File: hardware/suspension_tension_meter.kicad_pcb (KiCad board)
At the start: 2 copper layers, 63 parts, among them J1 Conn_01x04, J2 Conn_01x06, J3 Conn_01x04, J4 Conn_01x04, SW1 Tactswitch, U1 STM32L4P5RET6, U2 LM2596S-ADJ, U3 LM1117-5.0, U4 LM1117-3.3, U5 NAU7802SGI, U6 ATA6561, U7 NAU7802SGI, Y1 16MHz

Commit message: Arrange footprints
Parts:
- removed JP1: Terminator, Connector_PinHeader_2.54mm:PinHeader_1x02_P2.54mm_Vertical
- added C30: 1μF, Capacitor_SMD:C_0603_1608Metric, F.Cu at (171.3, 126.4)
- added J5: Terminator, Connector_PinHeader_2.54mm:PinHeader_1x02_P2.54mm_Vertical_SMD_Pin1Left, F.Cu at (127.4, 97.0)
- added R15: 51Ω, Resistor_SMD:R_0603_1608Metric, F.Cu at (175.2, 121.8)
- added REF**: MountingHole_4mm_Pad_Via, MountingHole:MountingHole_4mm_Pad_Via, F.Cu at (112.0, 84.0)
- added REF**: MountingHole_4mm_Pad_Via, MountingHole:MountingHole_4mm_Pad_Via, F.Cu at (186.0, 126.0)
- added REF**: MountingHole_4mm_Pad_Via, MountingHole:MountingHole_4mm_Pad_Via, F.Cu at (186.0, 84.0)
- added REF**: MountingHole_4mm_Pad_Via, MountingHole:MountingHole_4mm_Pad_Via, F.Cu at (112.0, 126.0)
- C1, C2: value 22pF -> 100nF
- C10: value 220μF -> 10nF; footprint Capacitor_SMD:CP_Elec_10x10 -> Capacitor_SMD:C_0603_1608Metric
- C11: value 100nF -> 10μF; footprint Capacitor_SMD:C_0603_1608Metric -> Capacitor_SMD:C_Elec_4x5.4
- C19: value 10μF -> 100nF; footprint Capacitor_SMD:CP_Elec_5x5.4 -> Capacitor_SMD:C_0603_1608Metric
- C20: value 100nF -> 10μF
- C24: value 470pF -> 100nF
- C26: value 100nF -> 470pF
- C29: value 1μF -> 100nF
- C7, C8: value 100nF -> 22pF
- C9: value 680μF -> 4.7μF; footprint Capacitor_SMD:CP_Elec_10x10 -> Capacitor_SMD:C_Elec_4x5.4
- D1: value 1N5822 -> SK32SMA; footprint Diode_THT:D_DO-201AD_P15.24mm_Horizontal -> Diode_SMD:D_SMA
- F1: footprint Fuse:Fuse_0603_1608Metric -> Fuse:Fuse_1210_3225Metric
- FB1, FB2: value 60R@100MHz -> 50mΩ@100MHz; footprint Inductor_SMD:L_0603_1608Metric -> Inductor_SMD:L_1206_3216Metric
- J1: footprint Connector_PinHeader_1.00mm:PinHeader_1x04_P1.00mm_Vertical_SMD_Pin1Left -> Connector_Wire:SolderWire-0.25sqmm_1x04_P4.2mm_D0.65mm_OD1.7mm_Relief
- J2: footprint Connector_PinHeader_1.00mm:PinHeader_1x06_P1.00mm_Vertical_SMD_Pin1Left -> Connector_PinHeader_2.54mm:PinHeader_1x06_P2.54mm_Vertical_SMD_Pin1Left
- J3, J4: footprint Connector_PinHeader_1.00mm:PinHeader_1x04_P1.00mm_Vertical_SMD_Pin1Left -> Connector_JST:JST_EH_S5B-EH_1x05_P2.50mm_Horizontal
- L1: value 33μH -> 2.2μH; footprint Inductor_SMD:L_0805_2012Metric -> Inductor_SMD:L_Bourns-SRN4018
- R1: value 100kΩ -> 330Ω
- R10, R9: value 51Ω -> 10kΩ
- R12: value 10kΩ -> 51Ω
- R3: value 330Ω -> 100kΩ
- R4: value 4.7kΩ -> 10kΩ
- R5: value 1kΩ -> 33kΩ
- R6: value 120Ω -> 4.7kΩ
- R7: value 10kΩ -> 120Ω
- SW1: footprint Button_Switch_SMD:SW_Push_1P1T_NO_6x6mm_H9.5mm -> Button_Switch_SMD:SW_SPST_PTS645
- U2: value LM2596S-ADJ -> AOZ1280CI; footprint Package_TO_SOT_SMD:TO-263-5_TabPin3 -> Package_TO_SOT_SMD:SOT-23-6
- U3, U4: footprint Package_TO_SOT_SMD:SOT-223 -> Package_TO_SOT_SMD:SOT-223-3_TabPin2
- U5: value NAU7802SGI -> ATA6561-GAQW-N; footprint Package_SO:SOIC-16_3.9x9.9mm_P1.27mm -> Package_SO:SOIC-8_3.9x4.9mm_P1.27mm
- U6: value ATA6561 -> NAU7802SGI; footprint Package_SO:SOIC-8_3.9x4.9mm_P1.27mm -> Package_SO:SOIC-16_3.9x9.9mm_P1.27mm
- moved J4 81.5 mm to (184.8, 100.0), turned to -90 degrees
- moved U4 75.4 mm to (176.2, 87.7)
- moved R13 71.6 mm to (121.3, 117.5), turned to 180 degrees
- moved C23 69.4 mm to (122.0, 123.8), turned to -90 degrees
- moved R12 68.4 mm to (121.3, 115.5), turned to 180 degrees
- moved C18 65.7 mm to (132.5, 116.0), turned to -90 degrees
- moved R10 65.0 mm to (132.5, 123.3), turned to 90 degrees
- moved C28 63.0 mm to (125.0, 112.9)
- moved C14 62.6 mm to (170.3, 86.0), turned to -90 degrees
- moved C25 59.3 mm to (122.0, 120.3), turned to -90 degrees
- moved C13 58.5 mm to (170.3, 89.8), turned to 90 degrees
- moved R8 57.6 mm to (132.5, 119.5), turned to -90 degrees
- moved J2 57.2 mm to (170.3, 107.7), turned to -90 degrees
- moved SW1 56.1 mm to (172.0, 98.6)
- moved C20 55.8 mm to (149.5, 124.9)
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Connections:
- C1 pad 1: Net-(C1-Pad1) -> +3.3V
- C10 pad 2: GND -> Net-(C10-Pad2)
- C11 pad 1: Net-(C10-Pad1) -> /Power Supply/6.42V
- C12 pad 1: +5V -> /Power Supply/6.42V
- C14 pad 1: +3.3V -> +5V
- C15 pad 1: Net-(C15-Pad1) -> +3.3V
- C17 pad 1: +3.3V -> Net-(C17-Pad1)
- C2 pad 1: Net-(C2-Pad1) -> +3.3V
- C22 pad 1: Net-(C22-Pad1) -> +3.3V
- C24 pad 2: Net-(C24-Pad2) -> GND
- C26 pad 1: /A1+ -> Net-(C26-Pad1)
- C26 pad 2: /A1- -> Net-(C26-Pad2)
- C27 pad 1: /A2+ -> /A1+
- C27 pad 2: /A2- -> /A1-
- C29 pad 1: +3.3V -> /A2+
- C29 pad 2: GND -> /A2-
- C3 pad 1: /NRST -> +3.3V
- C6 pad 1: +3.3V -> /NRST
- C7 pad 1: +3.3V -> Net-(C7-Pad1)
- C8 pad 1: +3.3V -> Net-(C8-Pad1)
- D1 pad 1: Net-(D1-Pad1) -> Net-(C10-Pad2)
- FB1 pad 1: +5V -> +3.3V
- FB2 pad 1: +3.3V -> +5V
- FB2 pad 2: Net-(C15-Pad1) -> Net-(C17-Pad1)
- J2 pad 6: unconnected-(J2-Pad6) -> /SWO
- L1 pad 1: Net-(D1-Pad1) -> Net-(C10-Pad2)
- L1 pad 2: Net-(C10-Pad1) -> /Power Supply/6.42V
- R1 pad 1: GND -> /NRST
- R10 pad 1: Net-(R10-Pad1) -> +3.3V
- R10 pad 2: /A1- -> /SCLK1
- R11 pad 2: /SDIO2 -> /SCLK2
- R12 pad 1: +3.3V -> Net-(R12-Pad1)
- R12 pad 2: /SCLK2 -> /A1+
- R13 pad 2: /A2+ -> /A1-
- R14 pad 2: /A2- -> /A2+
- R3 pad 1: /NRST -> GND
- R4 pad 1: Net-(C10-Pad1) -> Net-(C9-Pad1)
- R5 pad 1: Net-(R4-Pad2) -> /Power Supply/6.42V
- R5 pad 2: GND -> /Power Supply/FB
- R6 pad 1: Net-(JP1-Pad2) -> /Power Supply/FB
- R6 pad 2: /CAN- -> GND
- R7 pad 1: +3.3V -> Net-(J5-Pad2)
- R7 pad 2: /SDIO1 -> /CAN-
- R8 pad 2: /SCLK1 -> /SDIO1
- R9 pad 1: Net-(R9-Pad1) -> +3.3V
- R9 pad 2: /A1+ -> /SDIO2
- SW1 pad 2: Net-(R3-Pad2) -> Net-(R1-Pad2)
- U1 pad 5: Net-(C1-Pad1) -> Net-(C7-Pad1)
- U1 pad 55: unconnected-(U1-Pad55) -> /SWO
- U1 pad 6: Net-(C2-Pad1) -> Net-(C8-Pad1)
- U1 pad 60: Net-(R1-Pad2) -> Net-(R3-Pad2)
- U2 pad 1: Net-(C9-Pad1) -> Net-(C10-Pad1)
- U2 pad 2: Net-(D1-Pad1) -> GND
- U2 pad 3: GND -> /Power Supply/FB
- U2 pad 5: GND -> Net-(C9-Pad1)
- U3 pad 3: Net-(C10-Pad1) -> /Power Supply/6.42V
- U5 pad 1: +3.3V -> /CAN_TX
- U5 pad 2: Net-(R9-Pad1) -> GND
- U5 pad 3: Net-(R10-Pad1) -> Net-(C17-Pad1)
- U5 pad 4: Net-(C24-Pad1) -> /CAN_RX
- U5 pad 5: Net-(C24-Pad2) -> Net-(C16-Pad1)
- U5 pad 6: Net-(C22-Pad1) -> /CAN-
- U5 pad 7: GND -> /CAN+
- U6 pad 1: /CAN_TX -> +3.3V
- U6 pad 2: GND -> Net-(R12-Pad1)
- U6 pad 3: Net-(C16-Pad1) -> Net-(R13-Pad1)
- U6 pad 4: /CAN_RX -> Net-(C25-Pad1)
- U6 pad 5: Net-(C15-Pad1) -> Net-(C25-Pad2)
- U6 pad 6: /CAN- -> Net-(C23-Pad1)
- U6 pad 7: /CAN+ -> GND
- U7 pad 2: Net-(R13-Pad1) -> Net-(R14-Pad1)
- U7 pad 3: Net-(R14-Pad1) -> Net-(R15-Pad1)
- U7 pad 4: Net-(C25-Pad1) -> Net-(C26-Pad1)
- U7 pad 5: Net-(C25-Pad2) -> Net-(C26-Pad2)
- U7 pad 6: Net-(C23-Pad1) -> Net-(C24-Pad1)
- Y1 pad 1: Net-(C2-Pad1) -> Net-(C8-Pad1)
- Y1 pad 3: Net-(C1-Pad1) -> Net-(C7-Pad1)
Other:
- board outline added: 86 x 54 mm
- board text added: "LEFT"
- board text added: "RIGHT"
- board text added: "Rev: ${REVISION}"
- board text added: "Suspension Tension Meter"
- board text added: "‹Per aspera ad astra›"

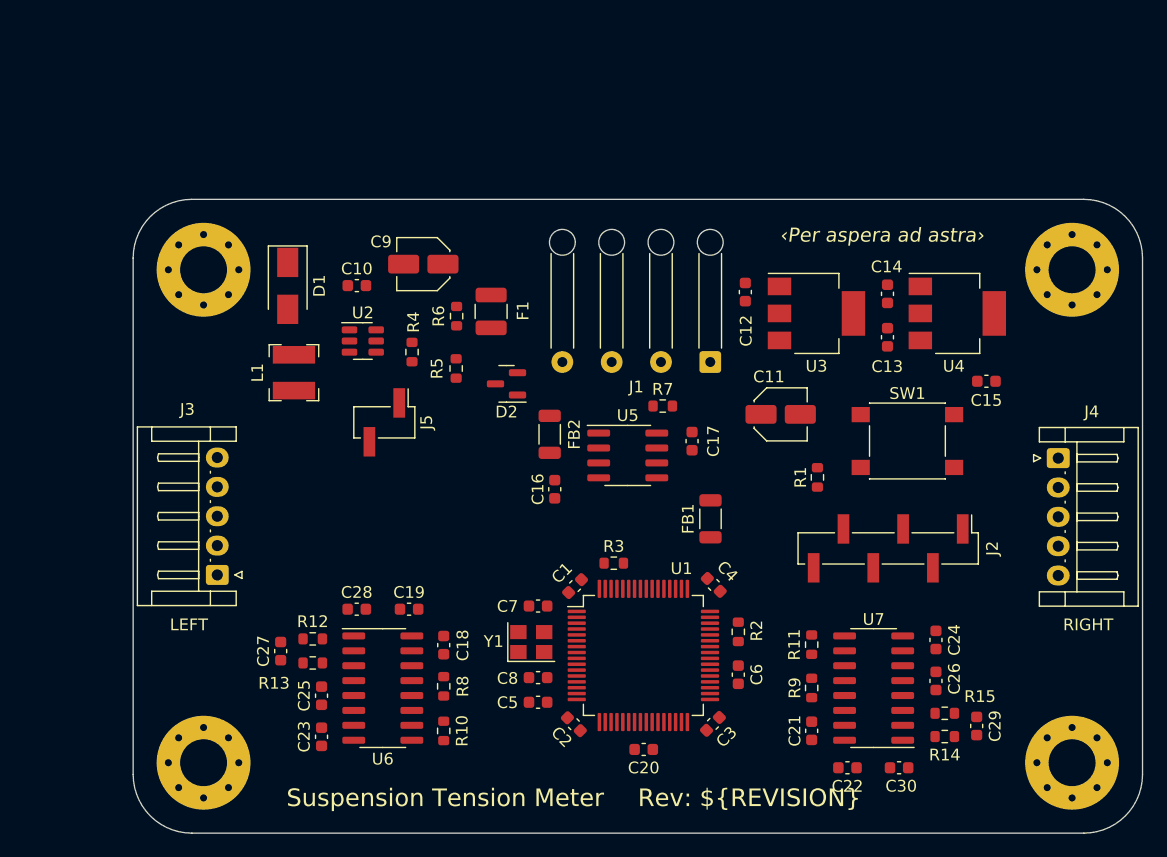
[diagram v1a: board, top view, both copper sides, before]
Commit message: Make the PCB more compact
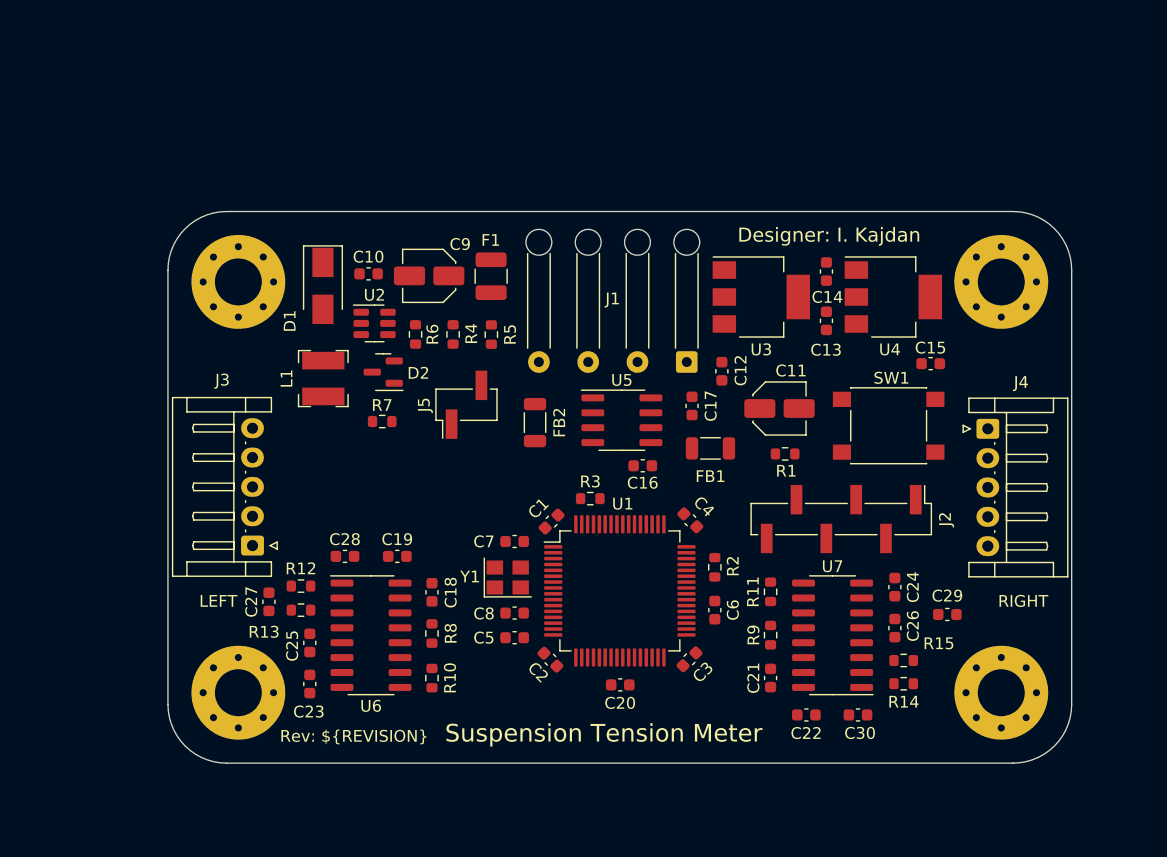
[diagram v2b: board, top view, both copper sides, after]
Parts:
- moved REF** 41.4 mm to (180.0, 85.0)
- moved REF** 36.5 mm to (180.0, 120.0)
- moved R7 23.9 mm to (127.2, 96.9), turned to 180 degrees
- moved D2 10.5 mm to (127.3, 92.7)
- moved C29 9.82 mm to (175.4, 113.4), turned to 180 degrees
- moved C16 7.76 mm to (149.4, 100.7), turned to 180 degrees
- moved J5 7.16 mm to (134.4, 95.5), turned to 90 degrees
- moved C12 7.04 mm to (156.2, 92.7), turned to -90 degrees
- moved REF** 6.66 mm to (115.0, 120.0)
- moved J4 6.50 mm to (178.8, 97.5)
- moved FB1 6.00 mm to (155.2, 99.2), turned to 180 degrees
- moved C1 5.85 mm to (141.7, 105.5)
- moved C2 5.85 mm to (141.6, 117.2)
- moved C20 5.85 mm to (147.5, 119.4)
- moved C3 5.85 mm to (153.4, 117.2)
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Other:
- board size 86 x 54 mm -> 77 x 47 mm
- board text added: "Designer: I. Kajdan"
- board text removed: "‹Per aspera ad astra›"

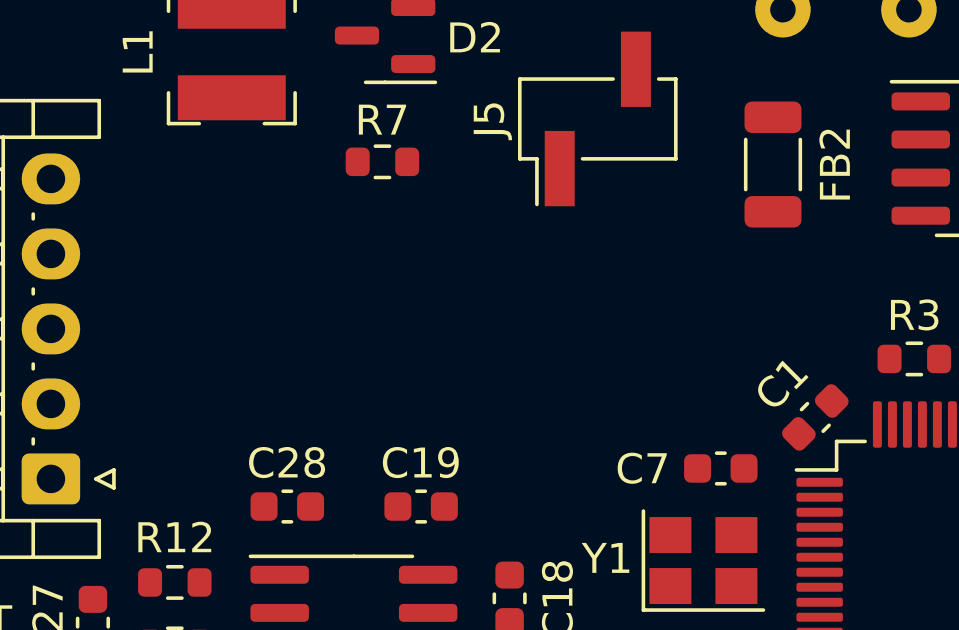
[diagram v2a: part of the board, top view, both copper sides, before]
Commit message: Apply PUTM branding
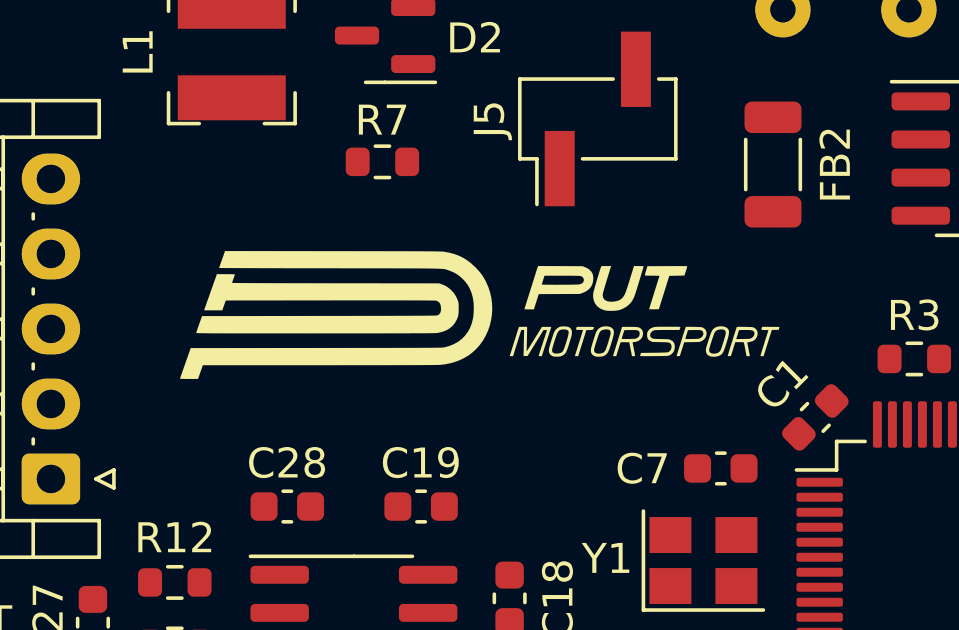
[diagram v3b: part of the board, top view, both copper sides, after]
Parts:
- added G***: LOGO, Local_Library:putm_text_20mm, F.Cu at (130.5, 102.0)

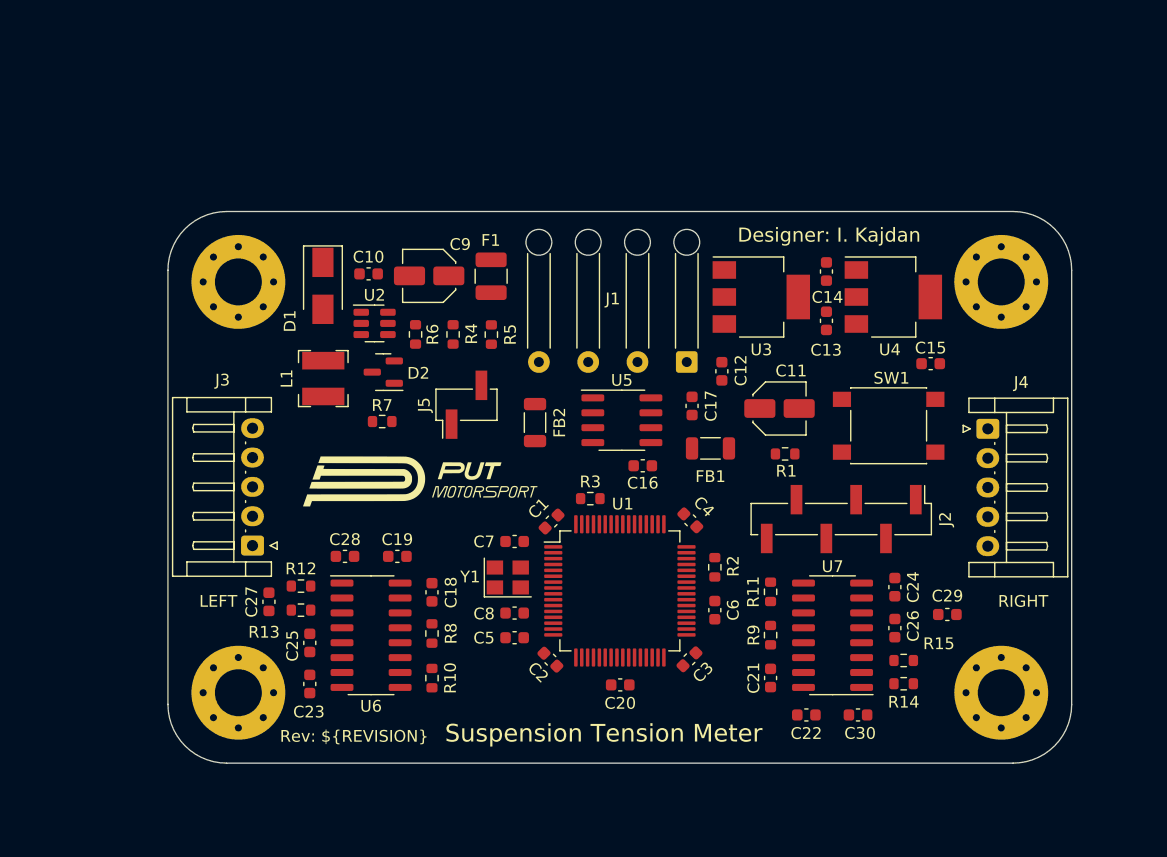
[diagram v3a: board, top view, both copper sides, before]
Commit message: Miscellaneous changes
- Use THT connectors
- Adjust ADC circuit according to the datasheet
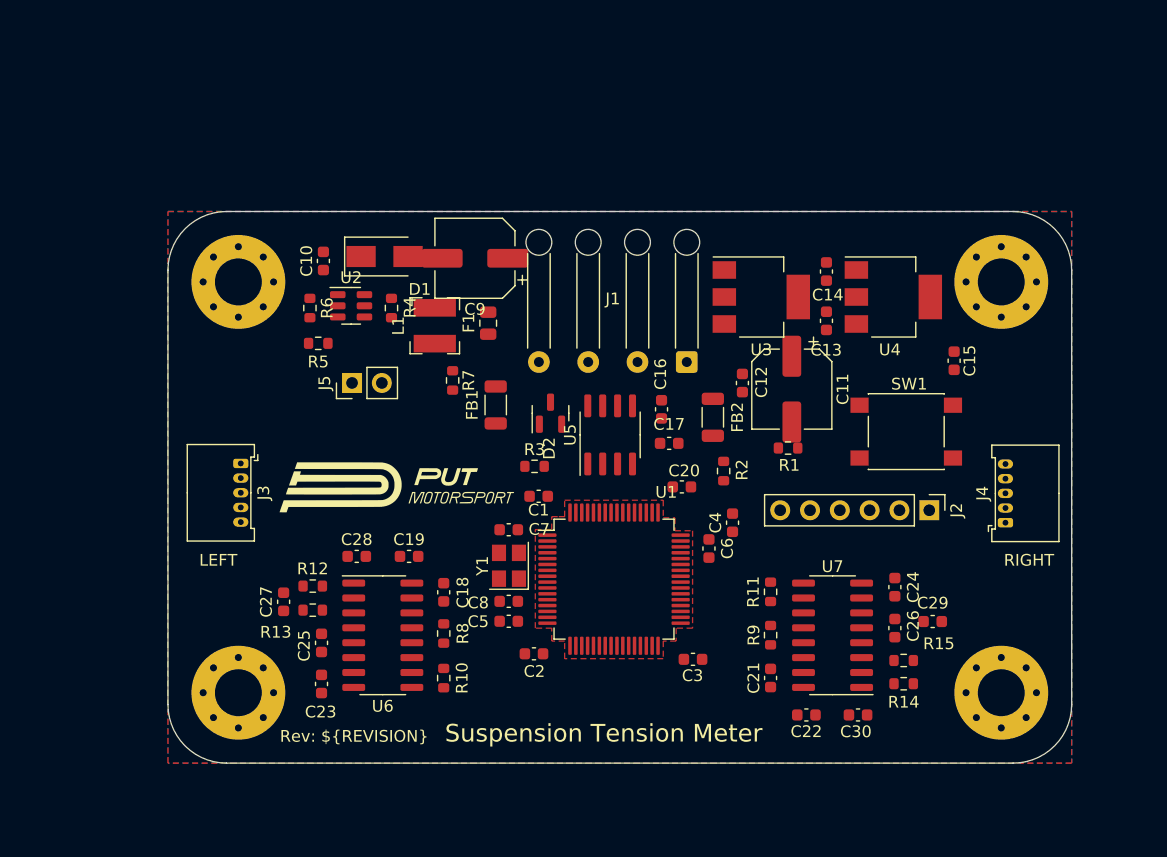
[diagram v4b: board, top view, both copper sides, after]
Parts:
- removed the G*** at (130.5, 102.0)
- added G***: LOGO, Local_Library:LogoText20mm, F.Cu at (128.5, 102.5)
- added G***: LOGO, Local_Library:SignatureBox25mm, B.Cu at (157.5, 115.5)
- added G***: LOGO, Local_Library:Rocket20mm, B.Cu at (131.0, 113.0)
- C11, C9: footprint Capacitor_SMD:C_Elec_4x5.4 -> Capacitor_SMD:CP_Elec_6.3x5.4
- C25, C26: value 470pF -> 330pF
- D1: value SK32SMA -> SK36A
- F1: footprint Fuse:Fuse_1210_3225Metric -> Fuse:Fuse_0805_2012Metric
- J2: footprint Connector_PinHeader_2.54mm:PinHeader_1x06_P2.54mm_Vertical_SMD_Pin1Left -> Connector_PinHeader_2.54mm:PinHeader_1x06_P2.54mm_Vertical
- J3, J4: footprint Connector_JST:JST_EH_S5B-EH_1x05_P2.50mm_Horizontal -> Connector_Molex:Molex_PicoBlade_53048-0510_1x05_P1.25mm_Horizontal
- J5: footprint Connector_PinHeader_2.54mm:PinHeader_1x02_P2.54mm_Vertical_SMD_Pin1Left -> Connector_PinHeader_2.54mm:PinHeader_1x02_P2.54mm_Vertical
- R10, R11, R8, R9: value 10kΩ -> 4.7kΩ
- R2, R3: value 100kΩ -> 10kΩ
- moved FB1 18.7 mm to (136.9, 95.5), turned to 90 degrees
- moved C20 17.7 mm to (152.8, 102.5), turned to 180 degrees
- moved FB2 15.2 mm to (155.4, 96.6)
- moved R5 14.8 mm to (121.8, 90.3), turned to 180 degrees
- moved D2 14.7 mm to (141.6, 96.2), turned to 90 degrees
- moved L1 10.5 mm to (131.7, 88.8)
- moved J5 9.92 mm to (124.7, 93.6)
- moved R6 9.28 mm to (121.1, 87.3)
- moved R2 8.23 mm to (156.3, 101.2)
- moved J4 8.14 mm to (180.3, 105.5), turned to 90 degrees
- moved J2 7.54 mm to (173.8, 104.5)
- moved J3 7.07 mm to (115.2, 100.5), turned to -90 degrees
- moved R7 6.95 mm to (133.2, 93.4), turned to 90 degrees
- moved D1 5.81 mm to (127.4, 82.9), turned to 0 degrees
- moved R4 5.71 mm to (128.0, 87.3)
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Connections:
- C27 pad 1: /A1+ -> Net-(C27-Pad1)
- C27 pad 2: /A1- -> Net-(C27-Pad2)
- C29 pad 1: /A2+ -> Net-(C29-Pad1)
- C29 pad 2: /A2- -> Net-(C29-Pad2)
- J1 pad 2: GND -> /CAN+
- J1 pad 3: /CAN+ -> /CAN-
- J1 pad 4: /CAN- -> GND
- R12 pad 1: Net-(R12-Pad1) -> Net-(C27-Pad1)
- R13 pad 1: Net-(R13-Pad1) -> Net-(C27-Pad2)
- R14 pad 1: Net-(R14-Pad1) -> Net-(C29-Pad1)
- R15 pad 1: Net-(R15-Pad1) -> Net-(C29-Pad2)
- U1 pad 10: unconnected-(U1-Pad10) -> /DRDY1
- U1 pad 27: /DRDY1 -> unconnected-(U1-Pad27)
- U1 pad 28: /DRDY2 -> unconnected-(U1-Pad28)
- U1 pad 29: /SCLK1 -> unconnected-(U1-Pad29)
- U1 pad 30: /SDIO1 -> unconnected-(U1-Pad30)
- U1 pad 36: unconnected-(U1-Pad36) -> /DRDY2
- U1 pad 44: /CAN_RX -> unconnected-(U1-Pad44)
- U1 pad 45: /CAN_TX -> unconnected-(U1-Pad45)
- U1 pad 61: unconnected-(U1-Pad61) -> /CAN_RX
- U1 pad 62: unconnected-(U1-Pad62) -> /CAN_TX
- U1 pad 8: unconnected-(U1-Pad8) -> /SCLK1
- U1 pad 9: unconnected-(U1-Pad9) -> /SDIO1
- U6 pad 2: Net-(R12-Pad1) -> Net-(C27-Pad1)
- U6 pad 3: Net-(R13-Pad1) -> Net-(C27-Pad2)
- U7 pad 2: Net-(R14-Pad1) -> Net-(C29-Pad1)
- U7 pad 3: Net-(R15-Pad1) -> Net-(C29-Pad2)
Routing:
- added copper zone on F.Cu, net +3.3V
- added copper zone on B.Cu, net GND
- added copper zone on F.Cu, net GND
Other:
- board text added: "IGNACY KAJDAN github.com/ikajdan"
- board text added: "‹Per aspera ad astra›"
- board text removed: "Designer: I. Kajdan"
